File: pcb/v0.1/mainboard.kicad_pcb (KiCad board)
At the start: 4 copper layers, 98.1 x 88.4 mm, 131 parts, among them J1 Conn_01x02_Pin, J11 Conn_01x03_Pin, J12 Conn_02x08_Odd_Even, J13 Conn_02x08_Odd_Even, J2 TYPE_C_Receptacle, J3 Conn_01x04_Pin, J4 TYPE_C_Receptacle, J5 TYPE_C_Receptacle, J6 22s_disp_connector, J7 ComputeModule5-CM5_connector, J8 Micro_SD_molex, J9 AudioJack3, Q1 MMBT2222A, SW1 SW_Push_45deg, U1 AP2112K-3.3TRG1, U2 Nexperia PUSB3FR4Z, U3 Nexperia PUSB3FR4Z, U4 PCM5102A, U5 RT9742GGJ5, U6 RT9742GGJ5, U7 MDBT50Q-P1MV2, U8 AP22653W6-7, Y1 O_32.768kHz

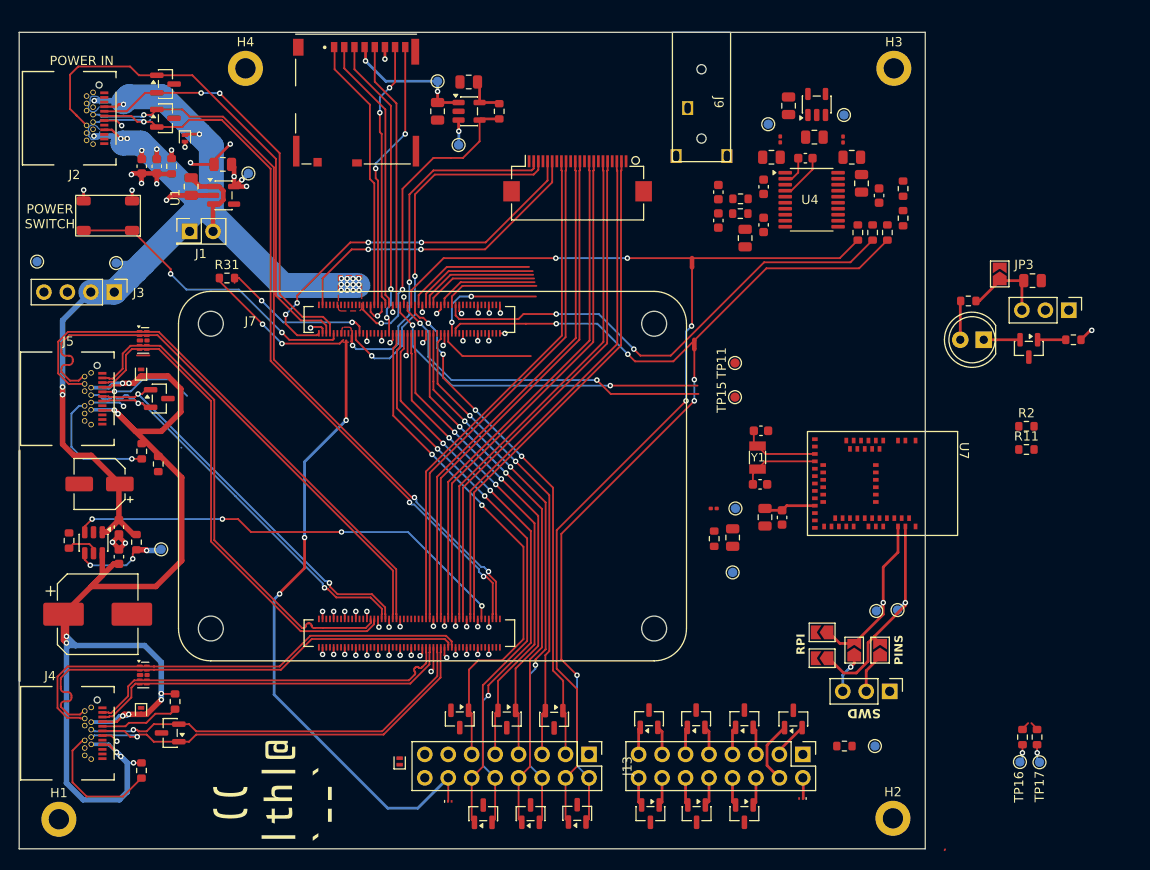
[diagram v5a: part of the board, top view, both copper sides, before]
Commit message: nRF wiring done
Both the wires from the raspberry to the nRF and nRF to gpio wires done.
That leaves only the dac and cleanup.
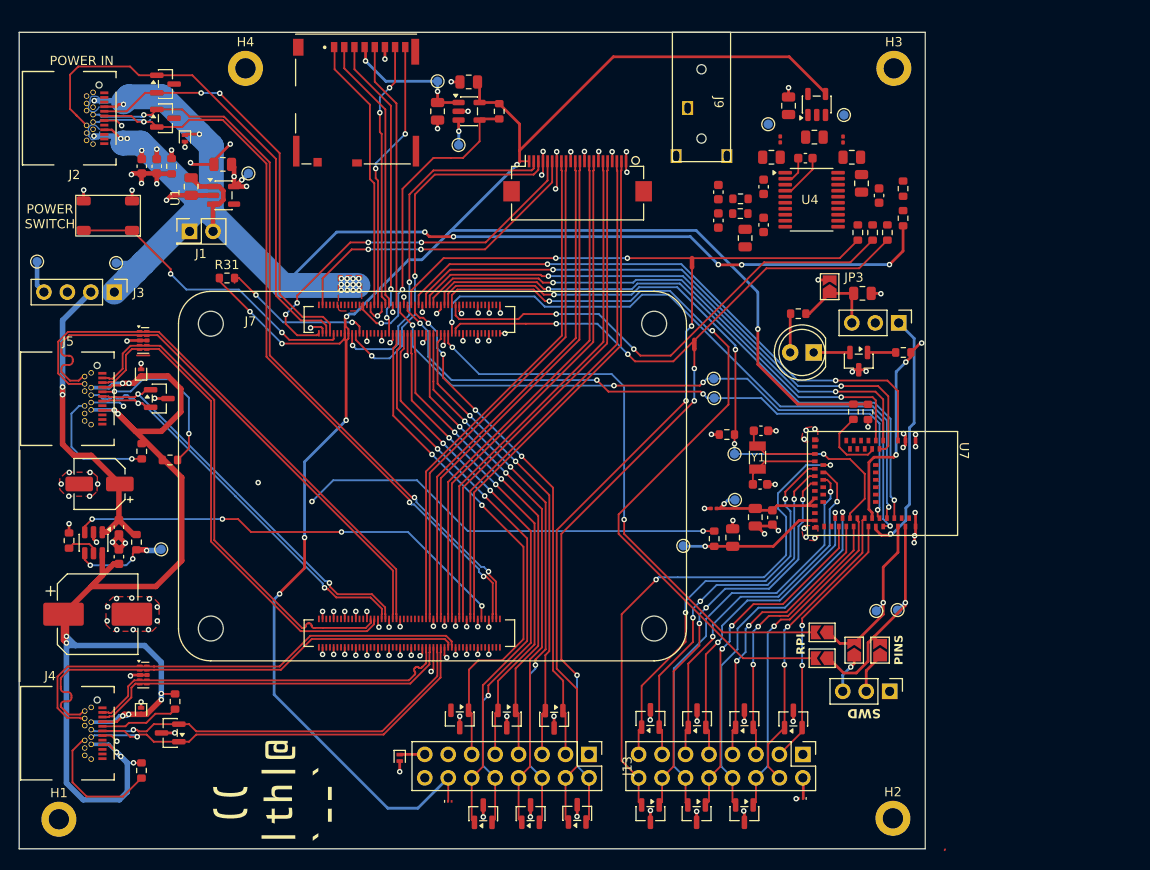
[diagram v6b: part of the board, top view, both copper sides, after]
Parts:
- removed R13, R14: 27R, Resistor_SMD:R_0603_1608Metric
- removed TP16, TP17: TestPoint, TestPoint:TestPoint_Pad_D1.0mm
- moved R15 36.0 mm to (100.2, 81.5)
- moved TP4 35.1 mm to (101.0, 83.5), turned to 90 degrees
- moved R2 18.8 mm to (113.9, 79.0), turned to 90 degrees
- moved R17 18.5 mm to (119.3, 72.6)
- moved S1 18.5 mm to (118.8, 69.4)
- moved C29 18.5 mm to (114.9, 66.2)
- moved D1 18.5 mm to (109.6, 72.6)
- moved JP3 18.5 mm to (111.3, 65.4)
- moved Q1 18.5 mm to (114.5, 73.5)
- moved R16 18.5 mm to (108.0, 68.4)
- moved R11 17.6 mm to (115.5, 79.0), turned to -90 degrees
- moved TP12 6.07 mm to (95.5, 93.5), turned to 90 degrees
- moved TP11 2.86 mm to (98.8, 75.4)
- moved TP15 2.25 mm to (98.8, 77.5)
- moved R23 1.34 mm to (39.9, 84.2), turned to 0 degrees
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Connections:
- D10 pad 1: /Co processor/GP0.07 -> /Co processor/GP0.19
- D10 pad 2: /Co processor/GP0.06 -> /Co processor/GP0.16
- D11 pad 1: /Co processor/GP0.26 -> /Co processor/GP0.15
- D11 pad 2: /Co processor/GP0.04/A2 -> /Co processor/GP0.17
- D12 pad 1: /Co processor/GP0.08 -> /Co processor/GP0.21
- D12 pad 2: /Co processor/GP0.05/A3 -> /Co processor/GP0.20
- D6 pad 1: /Co processor/GP0.13 -> /Co processor/GP0.05/A3
- D7 pad 1: /Co processor/GP0.15 -> /Co processor/GP0.04/A2
- D7 pad 2: /Co processor/GP0.16 -> /Co processor/GP0.06
- D8 pad 1: /Co processor/GP0.20 -> /Co processor/GP0.13
- D8 pad 2: /Co processor/GP0.21 -> /Co processor/GP0.07
- D9 pad 1: /Co processor/GP0.19 -> /Co processor/GP0.08
- D9 pad 2: /Co processor/GP0.17 -> /Co processor/GP0.26
- J12 pad 10: /Co processor/GP0.20 -> /Co processor/GP0.13
- J12 pad 11: /Co processor/GP0.13 -> /Co processor/GP0.05/A3
- J12 pad 12: /Co processor/GP0.21 -> /Co processor/GP0.07
- J12 pad 13: /Co processor/GP0.16 -> /Co processor/GP0.06
- J12 pad 14: /Co processor/GP0.19 -> /Co processor/GP0.08
- J12 pad 15: /Co processor/GP0.15 -> /Co processor/GP0.04/A2
- J12 pad 16: /Co processor/GP0.17 -> /Co processor/GP0.26
- J12 pad 3: /Co processor/GP0.05/A3 -> /Co processor/GP0.20
- J12 pad 4: /Co processor/GP0.08 -> /Co processor/GP0.21
- J12 pad 5: /Co processor/GP0.04/A2 -> /Co processor/GP0.17
- J12 pad 6: /Co processor/GP0.07 -> /Co processor/GP0.19
- J12 pad 7: /Co processor/GP0.26 -> /Co processor/GP0.15
- J12 pad 8: /Co processor/GP0.06 -> /Co processor/GP0.16
- R11 pad 1: /Co processor/+3v3_PI -> /+3v3_PI
- R2 pad 2: /Co processor/+3v3_PI -> /+3v3_PI
- U7 pad 3: /Co processor/MOD0 -> /Co processor/MOD3
- U7 pad 34: /Co processor/nRF_USB_N -> unconnected-(U7A-D--Pad34)
- U7 pad 35: /Co processor/nRF_USB_P -> unconnected-(U7A-D+-Pad35)
- U7 pad 49: /Co processor/U1_TX -> /Co processor/U1_RX
- U7 pad 50: /Co processor/U1_RX -> /Co processor/U1_TX
- U7 pad 6: /Co processor/MOD3 -> /Co processor/MOD0
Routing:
- net /+5v: track 121.8 -> 322.6 mm, vias 23 -> 31
- net /+3v3_PI: track 90.6 -> 227.7 mm, vias 5 -> 8
- net /Co processor/SWDCLK: track 10.5 -> 86.8 mm, vias 0 -> 2
- net /Co processor/nRESET: track 0.00 -> 68.3 mm, vias 0 -> 4
- net GND: track 76.5 -> 140.9 mm, vias 62 -> 135
- net /Co processor/U1_TX: track 11.2 -> 67.7 mm, vias 0 -> 2
- net /Co processor/U1_RX: track 12.6 -> 68.0 mm
- net /Co processor/GP0.26: track 3.07 -> 56.8 mm, vias 0 -> 2
- net /Co processor/SWDIO: track 10.5 -> 63.1 mm, vias 0 -> 2
- net /Co processor/MOD3: track 14.3 -> 65.4 mm, vias 0 -> 2
- net /Co processor/MOD2: track 13.8 -> 64.5 mm, vias 0 -> 2
- net /Co processor/MOD1: track 13.1 -> 61.2 mm, vias 0 -> 2
- net /Co processor/MOD0: track 12.5 -> 59.6 mm, vias 0 -> 2
- net /Co processor/GP0.07: track 3.06 -> 46.3 mm, vias 0 -> 1
- net /Co processor/GP0.04/A2: track 3.05 -> 43.5 mm, vias 0 -> 2
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- added copper zone on In2.Cu, net /+3v3_LDO
- added copper zone on F.Cu, net GND
- added copper zone on In1.Cu, net GND
- removed copper zone on F.Cu, net /+3v3_PI
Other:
- board text added: "labels for gpio"

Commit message: Draft 1 PCB complete!
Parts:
- moved TP1 1.95 mm to (106.6, 47.4)
- moved C23 1.69 mm to (106.9, 44.2)
- moved TP3 1.69 mm to (112.9, 45.2)
- moved C19 1.69 mm to (109.7, 47.6)
- moved U6 1.69 mm to (110.0, 44.0)
- moved R23 1.24 mm to (39.1, 83.2)
- moved FB2 0.90 mm to (106.9, 49.7)
- moved TP2 0.40 mm to (71.2, 49.7)
- moved C20 0.14 mm to (114.8, 54.1)
- moved C12 0.08 mm to (113.8, 51.3)
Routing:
- net GND: track 140.9 -> 194.1 mm, vias 135 -> 158
- net /GPIO/DAC_A_VDD: track 0.00 -> 16.7 mm, vias 0 -> 2
- net /GPIO/OUTL: track 0.00 -> 13.2 mm
- net /GPIO/XSMT: track 0.00 -> 12.4 mm
- net Net-(U6-VOUT): track 0.00 -> 12.3 mm, vias 0 -> 1
- net /GPIO/OUTR: track 0.00 -> 11.3 mm, vias 0 -> 1
- net /GPIO/LRCK: track 0.00 -> 6.33 mm
- net /GPIO/DIN: track 0.00 -> 4.46 mm
- net /GPIO/OUTR1: track 0.00 -> 4.25 mm
- net /GPIO/OUTL1: track 0.00 -> 4.19 mm
- net /GPIO/DAC_D_VDD: track 0.00 -> 3.50 mm
- net /+3v3_LDO: track 12.2 -> 15.6 mm
- net /GPIO/LDOO: track 0.00 -> 2.81 mm
- net /GPIO/BCK: track 0.00 -> 2.59 mm
- net /GPIO/VENG: track 0.00 -> 2.46 mm
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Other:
- board size 98.1 x 88.4 mm -> 98.1 x 88.7 mm
- board text added: "Audio"
- board text added: "Co-processor"
- board text added: "Display out"
- board text added: "Expansion Ports"
- board text added: "IR"
- board text added: "SD card"
- board text added: "nRF"

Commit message: Fixing up some DRC errors
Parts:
- added TP16: TestPoint, TestPoint:TestPoint_Pad_D1.0mm, F.Cu at (169.6, 89.3)
- moved TP7 78.6 mm to (111.6, 76.0), turned to 0 degrees
- moved C12 55.8 mm to (169.6, 53.1)
- moved C17 55.8 mm to (164.5, 53.3)
- moved C24 55.8 mm to (156.7, 94.3)
- moved C27 55.8 mm to (159.6, 88.6)
- moved C30 55.8 mm to (88.1, 88.5)
- moved D1 55.8 mm to (165.4, 74.3)
- moved D14 55.8 mm to (134.8, 124.2)
- moved D15 55.8 mm to (129.6, 124.2)
- moved D18 55.8 mm to (127.1, 114.0)
- moved D19 55.8 mm to (120.6, 118.2)
- moved D21 55.8 mm to (92.6, 113.1)
- moved D22 55.8 mm to (97.4, 51.1)
- moved D25 55.8 mm to (92.6, 76.5)
- moved D7 55.8 mm to (147.7, 113.9)
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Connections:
- J7 pad 51: /Co processor/U0_TX -> /Co processor/U0_RX
- J7 pad 55: /Co processor/U0_RX -> /Co processor/U0_TX
- TP7 pad 1: /+5v -> /+3v3_PI
- U7 pad 31: unconnected-(U7B-DCCH-Pad31) -> Net-(U7B-DCCH)
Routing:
- net /+5v: track 322.6 -> 328.2 mm, vias 31 -> 26
- net Net-(U7B-DCCH): track 0.00 -> 5.44 mm, vias 0 -> 2
- net /+3v3_PI: track 227.0 -> 231.1 mm, vias 8 -> 9
- net /Co processor/IR_TX: track 22.8 -> 21.2 mm, vias 3 -> 2
- net /Co processor/U0_RX: track 72.4 -> 71.5 mm
- net /Co processor/U0_TX: track 68.8 -> 69.5 mm
- net GND: vias 158 -> 425
- net /Co processor/GP0.08: vias 3 -> 2
- net /Co processor/GP0.06: vias 3 -> 2
- added copper zone on B.Cu, net GND
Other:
- board size 98.1 x 88.7 mm -> 98.2 x 88.7 mm
- board text added: "+3v3"
- board text added: "GP0.04"
- board text added: "GP0.05"
- board text added: "GP0.06"
- board text added: "GP0.07"
- board text added: "GP0.08"
- board text added: "GP0.13"
- board text added: "GP0.14"
- board text added: "GP0.15"
- board text added: "GP0.16"
- board text added: "GP0.17"
- board text added: "GP0.19"
- board text added: "GP0.21"
- board text added: "GP0.26"
- board text added: "GP02"
- board text added: "GP03"
- board text added: "GP04"
- board text added: "GP05"
- board text added: "GP11"
- board text added: "GP17"
- board text added: "GP18"
- board text added: "GP19"
- board text added: "GP23"
- board text added: "GP27"
- board text added: "GP9"
- board text removed: "Can make a silkscreen box around each group of components"
- board text removed: "comment"
- board text removed: "labels for gpio"
